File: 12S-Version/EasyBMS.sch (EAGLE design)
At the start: 149 parts, among them Q10 BSS84LT1G, Q11 BSS84LT1G, Q12 BSS84LT1G, Q13 BSS84LT1G, Q2 BSS84LT1G, Q3 BSS84LT1G, Q4 BSS84LT1G, Q5 BSS84LT1G, Q6 BSS84LT1G, Q7 BSS84LT1G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

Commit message: removed diode, connected V+ and C12+, GND and BAT-, improved routing for C1 - C4
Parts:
- removed D3: SM4007PL-TP, SamacSys_Parts:SM4007PL-TP
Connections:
- removed net C1-: C5.2, C6.2, D3.A, JP7.15_TOTAL-, R11.2, R3.2, R4.1
- removed net VIN: D2.K, JP7.1_TOTAL+, R15.2, R9.2, U$1.IN+
- net C1+: no longer D3.K
- net C12+: now also D2.K, JP7.1_TOTAL+, R15.2, R9.2, U$1.IN+
- net GND: now also C5.2, C6.2, JP7.15_TOTAL-, R11.2, R3.2, R4.1
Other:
- moved on the sheet: C1, C18, C19, C2, C20, C3, C4, D2, H1, H2, H3, JP10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

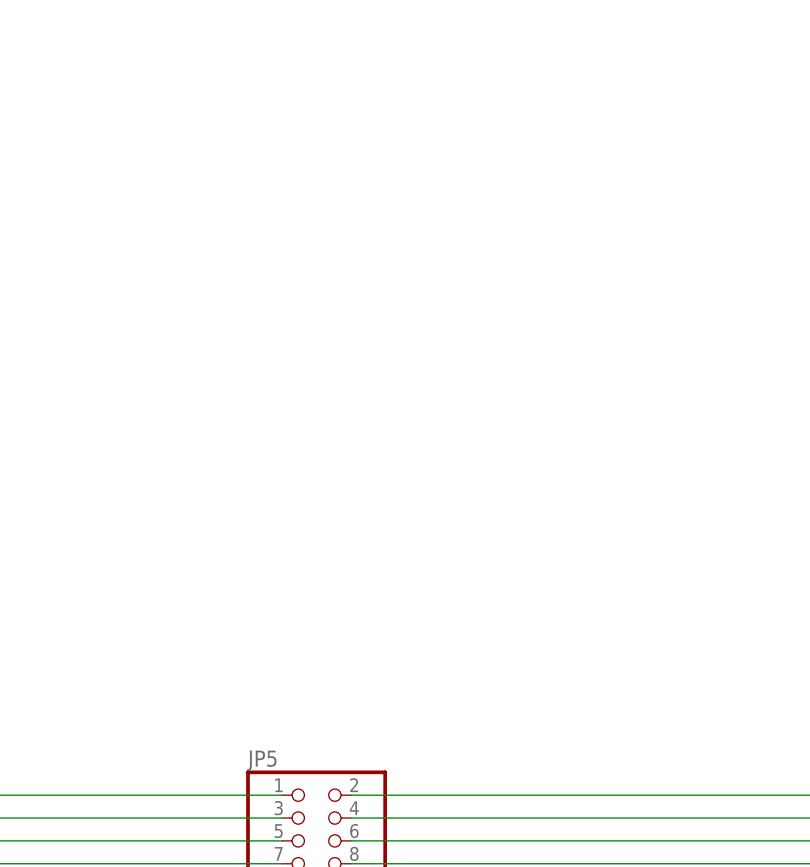
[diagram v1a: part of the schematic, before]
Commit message: SMD pinheader added as a part
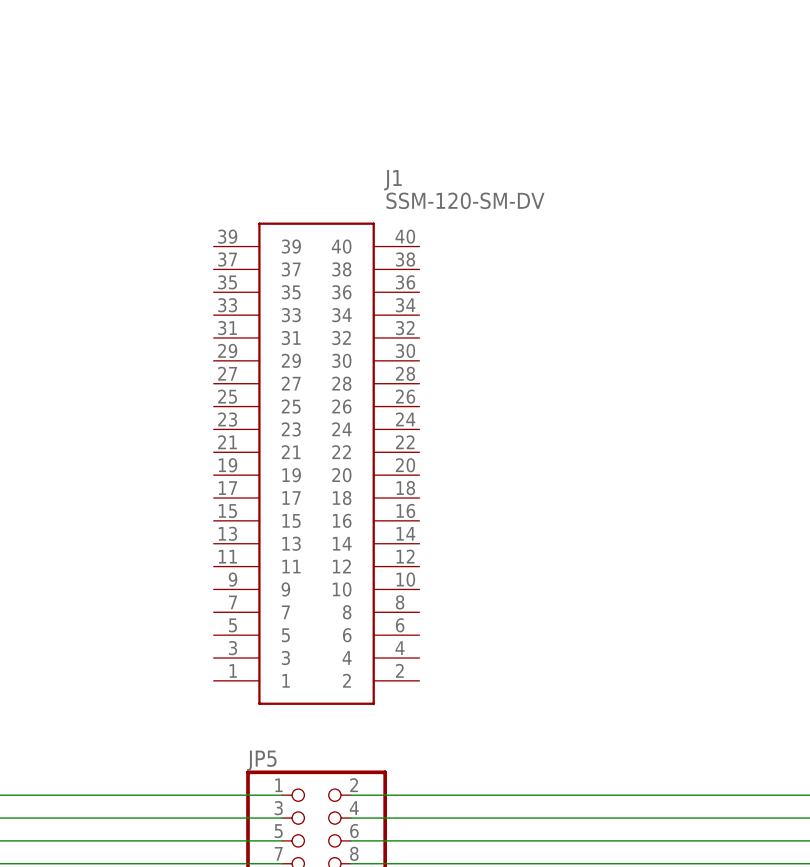
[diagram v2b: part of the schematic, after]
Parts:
- added J1: SSM-120-SM-DV, SamacSys_Parts:SSM-120-SM-DV
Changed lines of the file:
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@@
 <part name="R5" library="rcl" library_urn="urn:adsk.eagle:library:334" deviceset="R-EU_" device="R0603" package3d_urn="urn:adsk.eagle:package:23555/2" value="1k"/>
 <part name="R6" library="rcl" library_urn="urn:adsk.eagle:library:334" deviceset="R-EU_" device="R0603" package3d_urn="urn:adsk.eagle:package:23555/2" value="1k"/>
+<part name="J1" library="SamacSys_Parts" deviceset="SSM-120-SM-DV" device=""/>
 </parts>
 <sheets>
@@
 <attribute name="VALUE" x="100.33" y="315.722" size="1.778" layer="96" rot="R180"/>
 </instance>
+<instance part="J1" gate="G$1" x="-35.56" y="571.5" smashed="yes">
+<attribute name="NAME" x="-16.51" y="579.12" size="1.778" layer="95" align="center-left"/>
+<attribute name="VALUE" x="-16.51" y="576.58" size="1.778" layer="96" align="center-left"/>
+</instance>
 </instances>

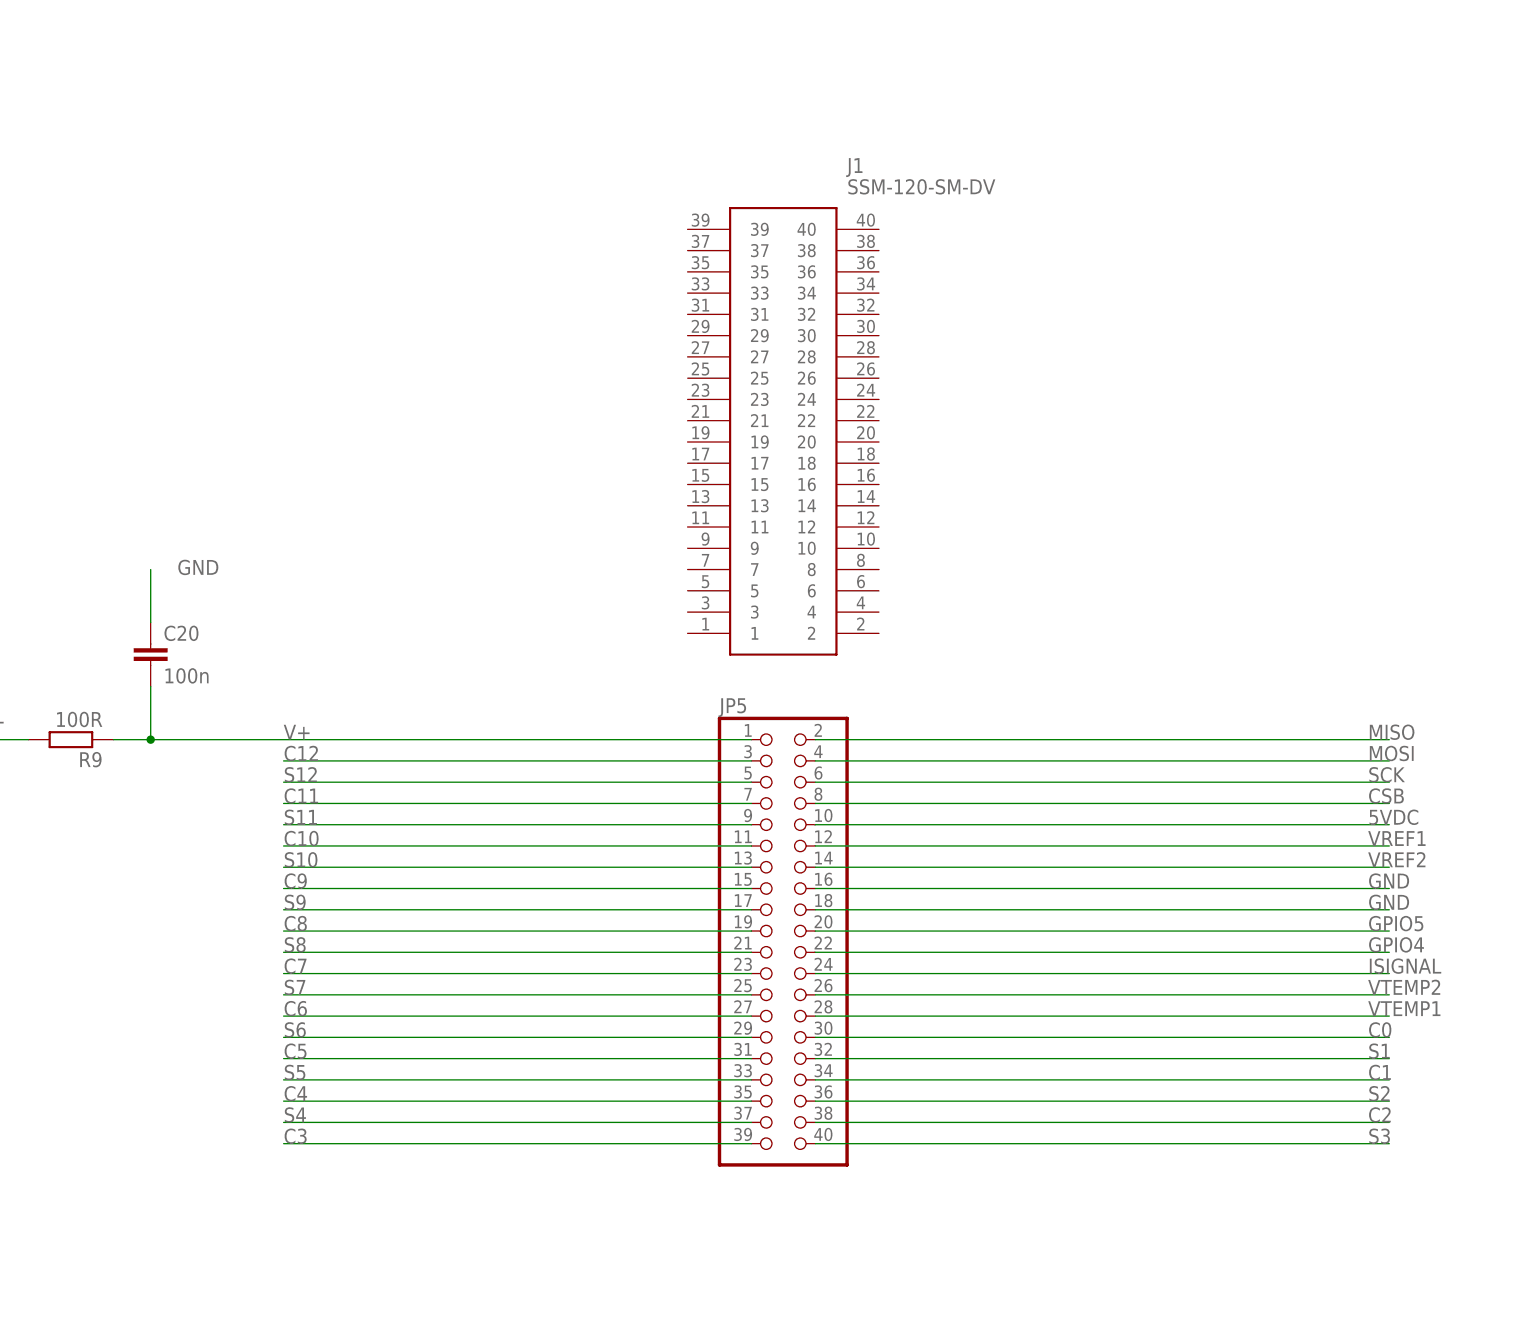
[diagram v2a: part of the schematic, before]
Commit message: SMD pinheader swaped but not placed
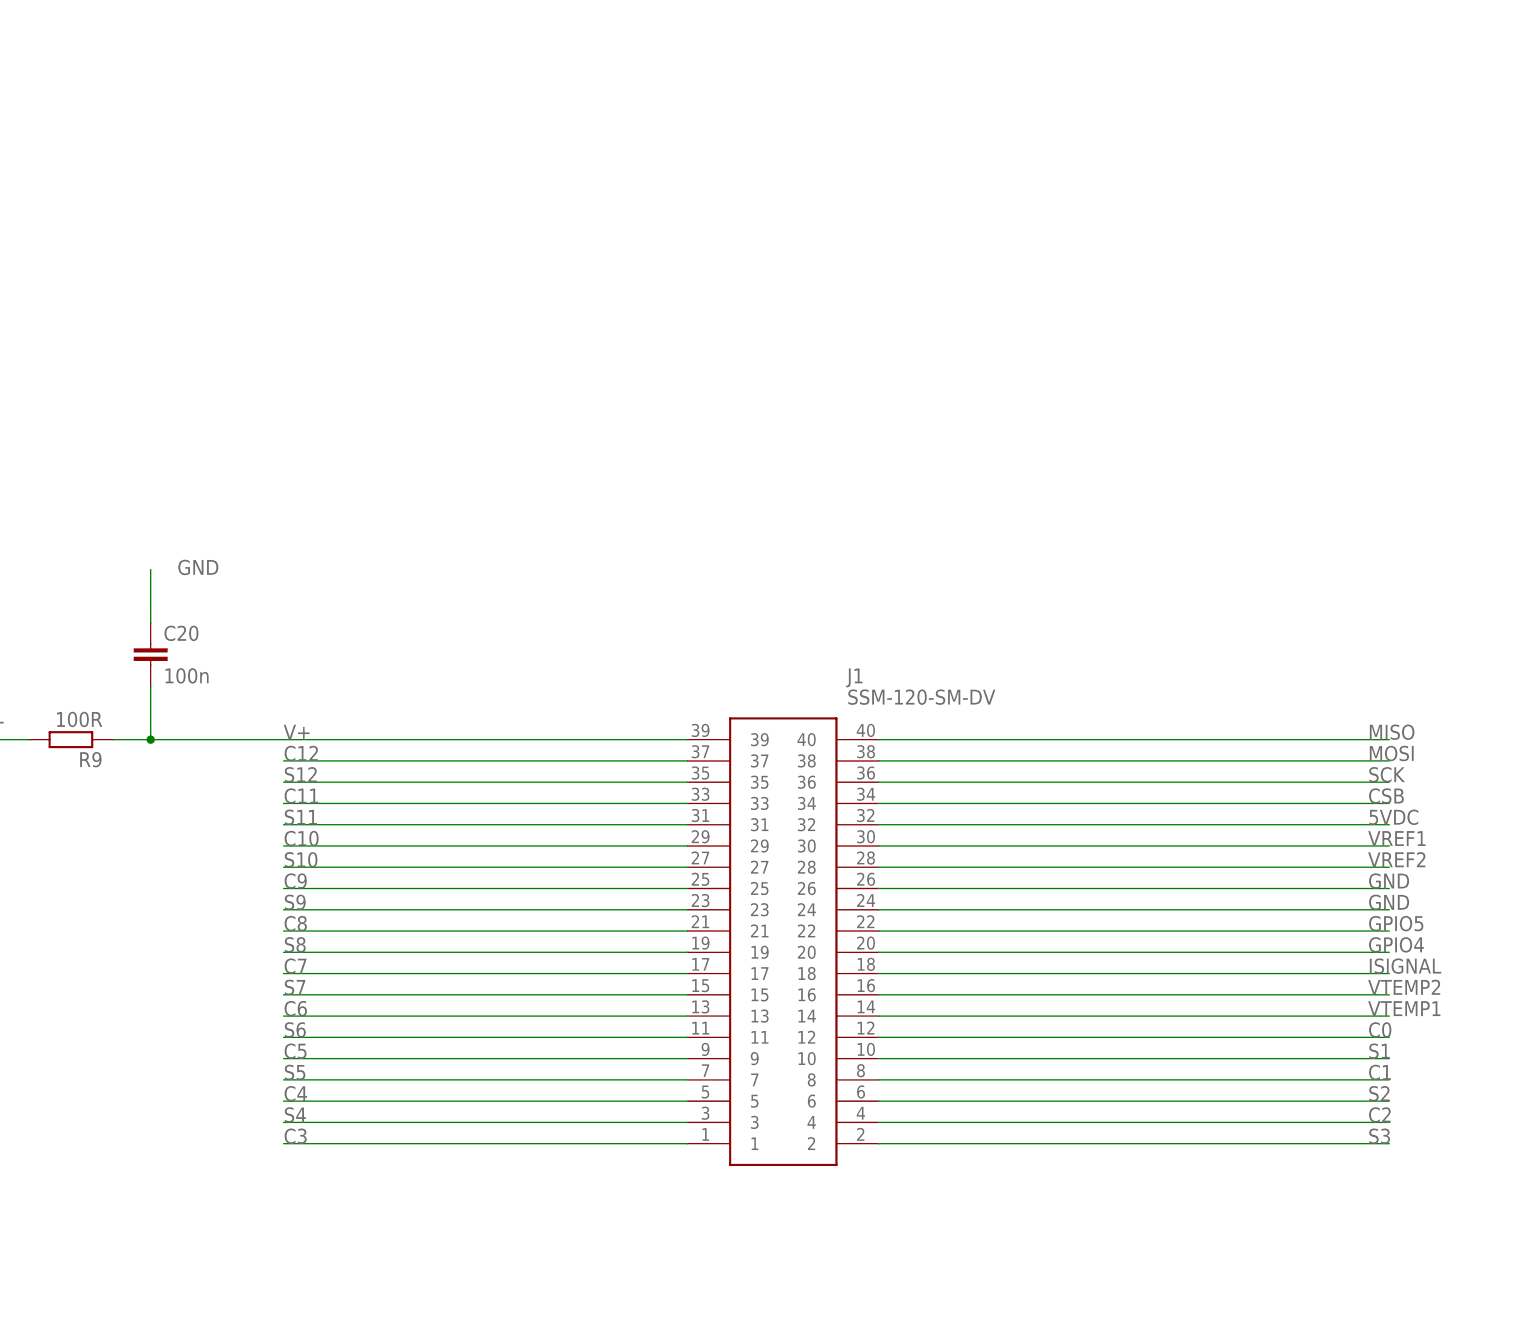
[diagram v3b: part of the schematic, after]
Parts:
- removed JP5: (no value), pinhead:PINHD-2X20
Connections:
- net 5VDC: now also J1.32; no longer JP5.10
- net C0: now also J1.12; no longer JP5.30
- net C1: now also J1.8; no longer JP5.34
- net C10: now also J1.29; no longer JP5.11
- net C11: now also J1.33; no longer JP5.7
- net C12: now also J1.37; no longer JP5.3
- net C2: now also J1.4; no longer JP5.38
- net C3: now also J1.1; no longer JP5.39
- net C4: now also J1.5; no longer JP5.35
- net C5: now also J1.9; no longer JP5.31
- net C6: now also J1.13; no longer JP5.27
- net C7: now also J1.17; no longer JP5.23
- net C8: now also J1.21; no longer JP5.19
- net C9: now also J1.25; no longer JP5.15
- net CSB: now also J1.34; no longer JP5.8
- net GND: now also J1.24, J1.26; no longer JP5.16, JP5.18
- net GPIO4: now also J1.20; no longer JP5.22
- net GPIO5: now also J1.22; no longer JP5.20
- net ISIGNAL: now also J1.18; no longer JP5.24
- net MISO: now also J1.40; no longer JP5.2
- net MOSI: now also J1.38; no longer JP5.4
- net S1: now also J1.10; no longer JP5.32
- net S10: now also J1.27; no longer JP5.13
- net S11: now also J1.31; no longer JP5.9
- net S12: now also J1.35; no longer JP5.5
- net S2: now also J1.6; no longer JP5.36
- net S3: now also J1.2; no longer JP5.40
- net S4: now also J1.3; no longer JP5.37
- net S5: now also J1.7; no longer JP5.33
- net S6: now also J1.11; no longer JP5.29
- net S7: now also J1.15; no longer JP5.25
- net S8: now also J1.19; no longer JP5.21
- net S9: now also J1.23; no longer JP5.17
- net SCK: now also J1.36; no longer JP5.6
- net V+: now also J1.39; no longer JP5.1
- net VREF1: now also J1.30; no longer JP5.12
- net VREF2: now also J1.28; no longer JP5.14
- net VTEMP1: now also J1.14; no longer JP5.28
- net VTEMP2: now also J1.16; no longer JP5.26
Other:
- moved on the sheet: J1
